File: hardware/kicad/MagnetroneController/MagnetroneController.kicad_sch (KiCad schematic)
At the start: 6 parts, among them J7 Conn_02x05_Odd_Even, J8 Conn_02x13_Counter_Clockwise

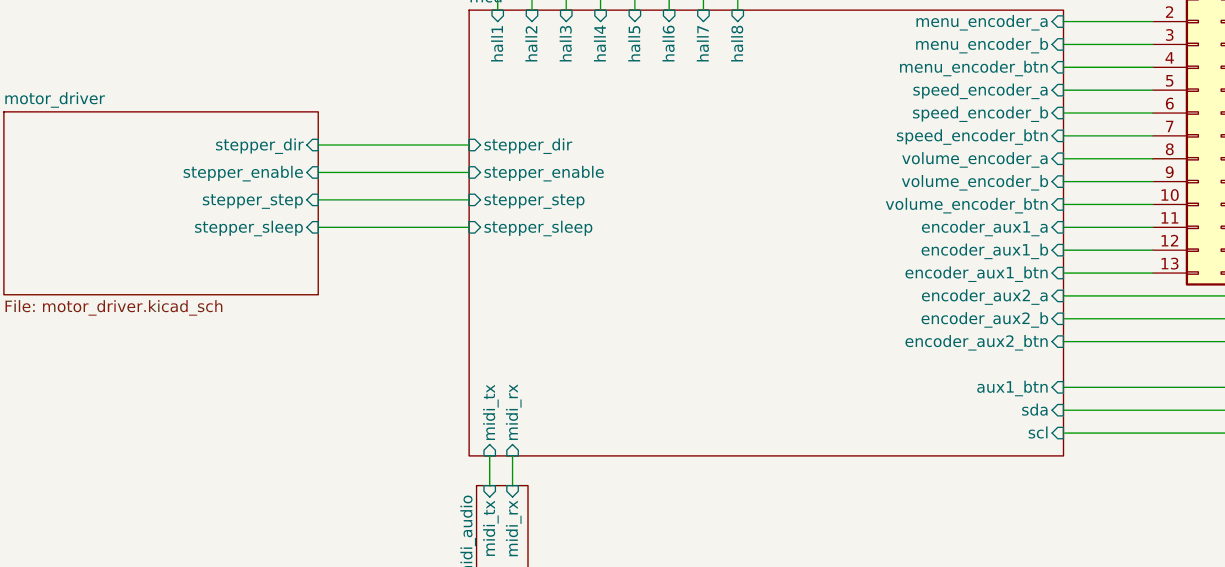
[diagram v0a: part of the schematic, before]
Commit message: chore: replace motor driver
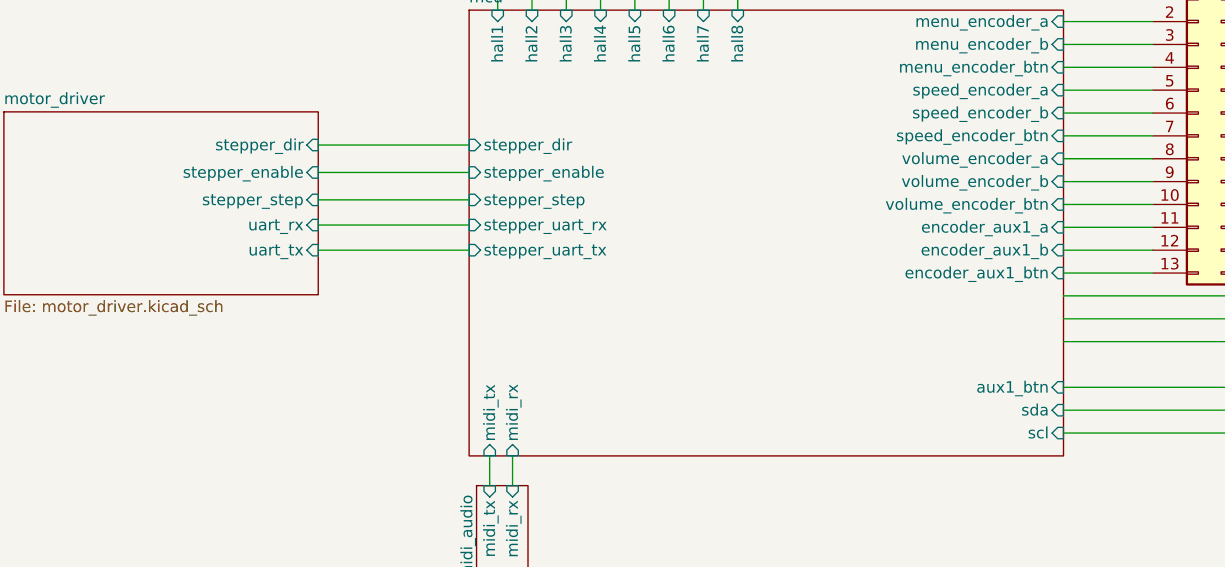
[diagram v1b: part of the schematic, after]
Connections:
- net mcu/encoder_aux2_a: no longer names the net of J8.14 (Pin_14)
- net mcu/encoder_aux2_b: no longer names the net of J8.15 (Pin_15)
- net mcu/encoder_aux2_btn: no longer names the net of J8.16 (Pin_16)
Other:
- sheet mcu ports: added stepper_uart_rx, stepper_uart_tx; removed encoder_aux2_a, encoder_aux2_b, encoder_aux2_btn, stepper_sleep
- sheet motor_driver ports: added uart_rx, uart_tx; removed stepper_sleep
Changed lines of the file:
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@@
-	(wire
-		(pts
-			(xy 64.77 89.662) (xy 81.534 89.662)
-		)
-		(stroke
-			(width 0)
-			(type default)
-		)
-	)
 	(wire
 		(pts
@@
 	(wire
 		(pts
+			(xy 64.77 89.408) (xy 81.534 89.408)
+		)
+		(stroke
+			(width 0)
+			(type default)
+		)
+	)
+	(wire
+		(pts
 			(xy 147.574 82.042) (xy 157.48 82.042)
 		)
@@
 		(pts
 			(xy 147.574 69.342) (xy 157.48 69.342)
+		)
+		(stroke
+			(width 0)
+			(type default)
+		)
+	)
+	(wire
+		(pts
+			(xy 64.77 92.202) (xy 81.534 92.202)
 		)
 		(stroke
@@
 		)
 		(instances
-			(project "MagnetronController"
+			(project "MagnetroneController"
 				(path "/a200339a-72b8-45b5-a453-e4d4f113bf3a"
 					(page "7")
@@
 			)
 		)
-		(pin "stepper_sleep" input
-			(at 64.77 89.662 0)
-			(effects
-				(font
-					(size 1.27 1.27)
-				)
-				(justify right)
-			)
-		)
 		(pin "stepper_step" input
 			(at 64.77 86.614 0)
@@
 			)
 		)
+		(pin "uart_rx" input
+			(at 64.77 89.408 0)
+			(effects
+				(font
+					(size 1.27 1.27)
+				)
+				(justify right)
+			)
+		)
+		(pin "uart_tx" input
+			(at 64.77 92.202 0)
+			(effects
+				(font
+					(size 1.27 1.27)
+				)
+				(justify right)
+			)
+		)
 		(instances
-			(project "MagnetronController"
+			(project "MagnetroneController"
 				(path "/a200339a-72b8-45b5-a453-e4d4f113bf3a"
 					(page "4")
@@
 		)
 		(instances
-			(project "MagnetronController"
+			(project "MagnetroneController"
 				(path "/a200339a-72b8-45b5-a453-e4d4f113bf3a"
 					(page "6")
@@
 			)
 		)
-		(pin "stepper_sleep" input
-			(at 81.534 89.662 180)
-			(effects
-				(font
-					(size 1.27 1.27)
-				)
-				(justify left)
-			)
-		)
 		(pin "encoder_aux1_a" input
 			(at 147.574 89.662 0)
@@
 			)
 		)
-		(pin "encoder_aux2_a" input
-			(at 147.574 97.282 0)
-			(effects
-				(font
-					(size 1.27 1.27)
-				)
-				(justify right)
-			)
-		)
-		(pin "encoder_aux2_b" input
-			(at 147.574 99.822 0)
-			(effects
-				(font
-					(size 1.27 1.27)
-				)
-				(justify right)
-			)
-		)
-		(pin "encoder_aux2_btn" input
-			(at 147.574 102.362 0)
-			(effects
-				(font
-					(size 1.27 1.27)
-				)
-				(justify right)
-			)
-		)
 		(pin "menu_encoder_a" input
 			(at 147.574 66.802 0)
@@
 			)
 		)
+		(pin "stepper_uart_rx" input
+			(at 81.534 89.408 180)
+			(effects
+				(font
+					(size 1.27 1.27)
+				)
+				(justify left)
+			)
+		)
+		(pin "stepper_uart_tx" input
+			(at 81.534 92.202 180)
+			(effects
+				(font
+					(size 1.27 1.27)
+				)
+				(justify left)
+			)
+		)
 		(instances
-			(project "MagnetronController"
+			(project "MagnetroneController"
 				(path "/a200339a-72b8-45b5-a453-e4d4f113bf3a"
 					(page "3")

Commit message: feat: cleanup
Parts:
- J8: footprint Connector_IDC:IDC-Header_2x13_P2.54mm_Horizontal -> Connector_IDC:IDC-Header_2x13_P2.54mm_Vertical
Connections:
- no-connect marks 5 -> 8
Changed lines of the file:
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@@
+	)
+	(no_connect
+		(at 170.18 94.742)
+	)
+	(no_connect
+		(at 170.18 89.662)
 	)
 	(no_connect
@@
 	)
 	(no_connect
+		(at 170.18 92.202)
+	)
+	(no_connect
 		(at 170.18 82.042)
 	)
@@
 	(wire
 		(pts
-			(xy 173.99 89.662) (xy 173.99 102.362)
-		)
-		(stroke
-			(width 0)
-			(type default)
-		)
-	)
-	(wire
-		(pts
 			(xy 111.379 46.99) (xy 111.379 65.532)
 		)
@@
 	(wire
 		(pts
-			(xy 171.9743 99.822) (xy 171.9743 92.202)
-		)
-		(stroke
-			(width 0)
-			(type default)
-		)
-	)
-	(wire
-		(pts
-			(xy 147.574 97.282) (xy 170.18 97.282)
-		)
-		(stroke
-			(width 0)
-			(type default)
-		)
-	)
-	(wire
-		(pts
 			(xy 84.709 29.21) (xy 84.709 65.532)
 		)
@@
 	(wire
 		(pts
-			(xy 173.99 102.362) (xy 147.574 102.362)
-		)
-		(stroke
-			(width 0)
-			(type default)
-		)
-	)
-	(wire
-		(pts
 			(xy 64.77 83.566) (xy 81.534 83.566)
 		)
@@
 	(wire
 		(pts
-			(xy 170.18 89.662) (xy 173.99 89.662)
-		)
-		(stroke
-			(width 0)
-			(type default)
-		)
-	)
-	(wire
-		(pts
 			(xy 138.43 41.91) (xy 103.759 41.91)
 		)
@@
 	(wire
 		(pts
-			(xy 147.574 99.822) (xy 171.9743 99.822)
-		)
-		(stroke
-			(width 0)
-			(type default)
-		)
-	)
-	(wire
-		(pts
 			(xy 136.525 29.21) (xy 142.24 29.21)
 		)
@@
 	(wire
 		(pts
-			(xy 170.18 97.282) (xy 170.18 94.742)
-		)
-		(stroke
-			(width 0)
-			(type default)
-		)
-	)
-	(wire
-		(pts
 			(xy 181.61 69.342) (xy 170.18 69.342)
-		)
-		(stroke
-			(width 0)
-			(type default)
-		)
-	)
-	(wire
-		(pts
-			(xy 171.9743 92.202) (xy 170.18 92.202)
 		)
 		(stroke
@@
 			)
 		)
-		(property "Footprint" "Connector_IDC:IDC-Header_2x13_P2.54mm_Horizontal"
+		(property "Footprint" "Connector_IDC:IDC-Header_2x13_P2.54mm_Vertical"
 			(at 162.56 79.502 0)
 			(effects
